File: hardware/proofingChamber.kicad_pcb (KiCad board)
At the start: 2 copper layers, 40 x 67.5 mm, 15 parts, among them J4 Conn_01x02, SW2 RotaryEncoder_Switch_MP, U1 ESP32-C3_SUPERMINI_TH, U2 DS18B20

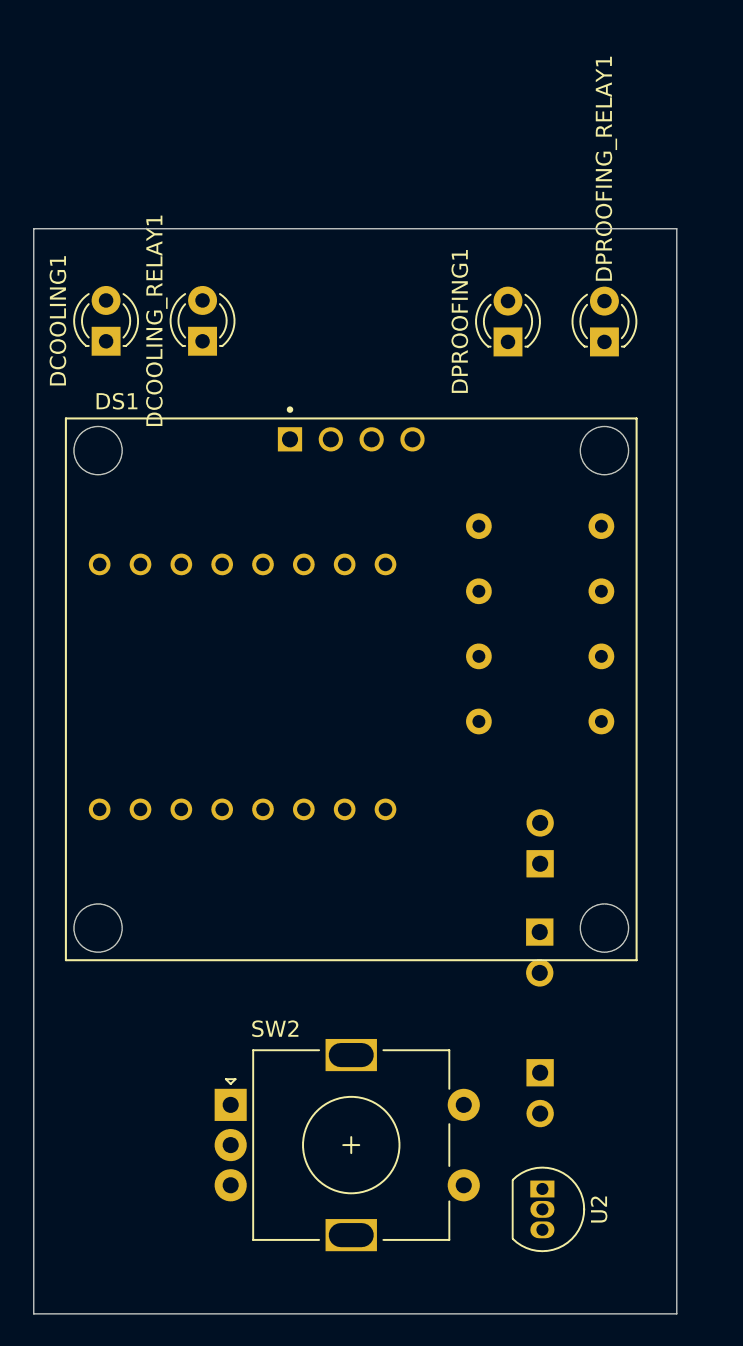
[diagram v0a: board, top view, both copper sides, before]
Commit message: Refactor hardware design files: remove obsolete proofingChamber.kicad_prl, update net classes and schematic connections
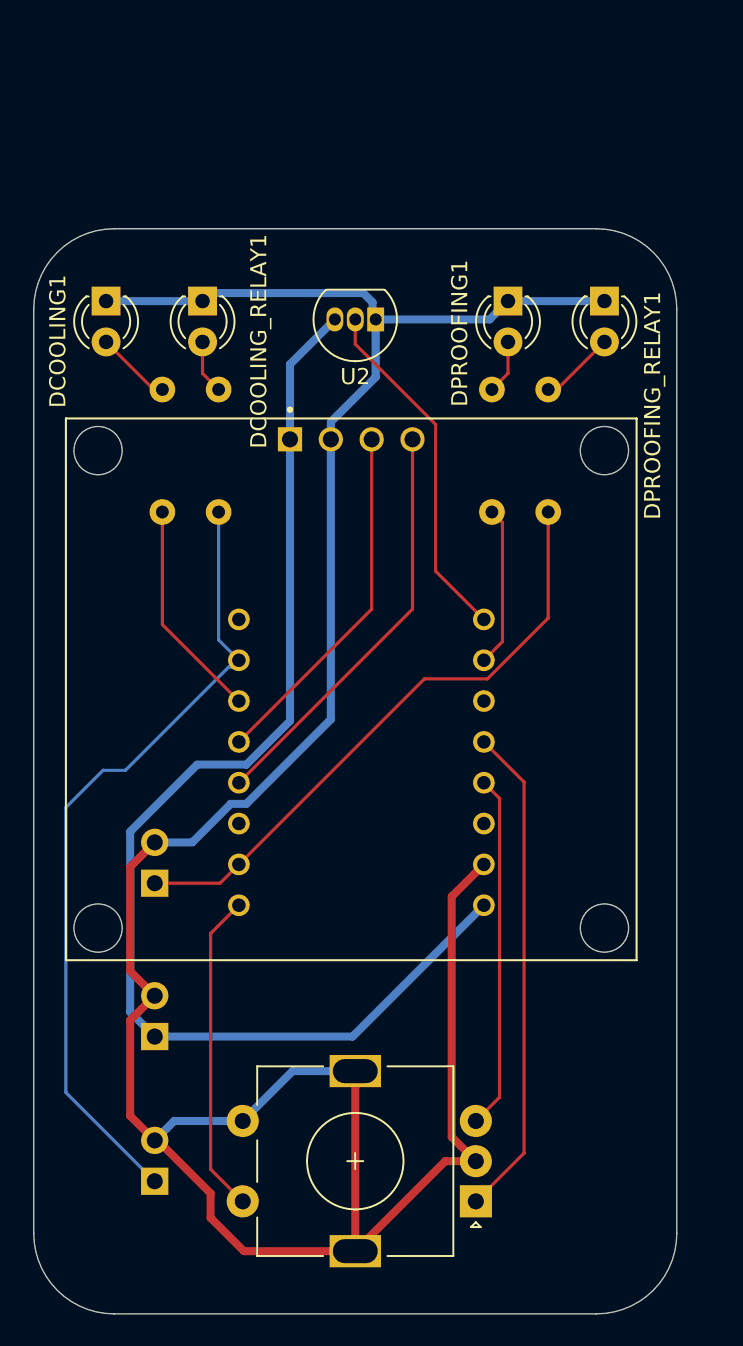
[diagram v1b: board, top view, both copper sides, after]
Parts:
- moved U2 55.1 mm to (238.8, 102.6), turned to 180 degrees
- moved RCOOLING_RELAY_LED1 31.5 mm to (229.0, 107.0), turned to -90 degrees
- moved JCOOLING1 28.5 mm to (225.0, 156.2), turned to 0 degrees
- moved JPOWER 24.1 mm to (225.0, 147.2), turned to 0 degrees
- moved JPROOFING 24.0 mm to (225.0, 137.7)
- moved RCOOLING_LED1 23.3 mm to (225.5, 107.0), turned to -90 degrees
- moved RPROOFING_RELAY_LED1 16.9 mm to (249.5, 107.0), turned to -90 degrees
- moved SW2 16.4 mm to (245.0, 157.5), turned to 180 degrees
- moved RPROOFING_LED1 10.9 mm to (246.0, 107.0), turned to -90 degrees
- moved U1 7.37 mm to (237.9, 129.2), turned to 0 degrees
- moved DPROOFING1 2.54 mm to (247.0, 101.5), turned to -90 degrees
- moved DPROOFING_RELAY1 2.54 mm to (253.0, 101.5), turned to -90 degrees
- moved DCOOLING1 2.50 mm to (222.0, 101.5), turned to -90 degrees
- moved DCOOLING_RELAY1 2.50 mm to (228.0, 101.5), turned to -90 degrees
- renumbered J4 to JPOWER, JPROOFING1 to JPROOFING
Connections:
- U1 pad 1: /COOLING_RELAY -> /PROOFING_LED
- U1 pad 2: /PROOFING_RELAY -> unconnected-(U1-GPIO2-Pad2)
- U1 pad 20: unconnected-(U1-GPIO20-Pad20) -> /COOLING_RELAY
- U1 pad 6: /PROOFING_LED -> /PROOFING_RELAY
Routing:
- net GND: track 0.00 -> 165.5 mm
- net +5V: track 0.00 -> 76.2 mm
- net /COOLING_RELAY: track 0.00 -> 49.8 mm
- net /PROOFING_RELAY: track 0.00 -> 37.5 mm
- net /ENCODER_A: track 0.00 -> 30.9 mm
- net /SDA: track 0.00 -> 25.8 mm
- net /SCK: track 0.00 -> 22.2 mm
- net /ENCODER_B: track 0.00 -> 22.1 mm
- net /DS18B22_PIN: track 0.00 -> 22.0 mm
- net /ENCODER_BTN: track 0.00 -> 20.0 mm
- net /COOLING_LED: track 0.00 -> 13.7 mm
- net /PROOFING_LED: track 0.00 -> 9.97 mm
- net Net-(DPROOFING_RELAY1-A): track 0.00 -> 4.73 mm
- net Net-(DCOOLING1-A): track 0.00 -> 4.73 mm
- net Net-(DPROOFING1-A): track 0.00 -> 3.37 mm
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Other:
- outline, holes or cut-outs redrawn

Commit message: Update PCB
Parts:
- removed DCOOLING_RELAY1, DPROOFING_RELAY1: LED, LED_THT:LED_D3.0mm
- removed JCOOLING1, JPOWER, JPROOFING: Conn_01x02, Connector_PinSocket_2.54mm:PinSocket_1x02_P2.54mm_Vertical
- removed RCOOLING_RELAY_LED1, RPROOFING_RELAY_LED1: R, Resistor_THT:R_Axial_DIN0207_L6.3mm_D2.5mm_P7.62mm_Horizontal
- removed U2: DS18B20, Package_TO_SOT_THT:TO-92_Inline
- added J1: Conn_02x06_Odd_Even, Connector_PinSocket_2.54mm:PinSocket_2x06_P2.54mm_Horizontal, B.Cu at (231.5, 131.8)
- added REF**: OSHW-Logo2_9.8x8mm_SilkScreen, Symbol:OSHW-Logo2_9.8x8mm_SilkScreen, B.Cu at (238.8, 154.0)
- moved DPROOFING1 54.1 mm to (253.0, 155.3), turned to 90 degrees
- moved DCOOLING1 53.8 mm to (224.0, 155.3), turned to 90 degrees
- moved RPROOFING_LED1 38.9 mm to (251.4, 145.5), turned to 180 degrees
- moved RCOOLING_LED1 38.5 mm to (225.5, 145.5), turned to 0 degrees
- moved SW2 15.0 mm to (231.2, 151.5), turned to 0 degrees
- moved U1 8.46 mm to (245.5, 125.5), turned to 90 degrees
- moved DS1 1.25 mm to (238.5, 125.7)
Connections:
- U1 pad 0: /DS18B22_PIN -> unconnected-(U1-GPIO0-Pad0)
- U1 pad 1: /PROOFING_LED -> /PROOFING_RELAY
- U1 pad 10: /COOLING_LED -> /PROOFING_LED
- U1 pad 2: unconnected-(U1-GPIO2-Pad2) -> /COOLING_RELAY
- U1 pad 20: /COOLING_RELAY -> /DS18B22_PIN
- U1 pad 21: unconnected-(U1-GPIO21-Pad21) -> /COOLING_LED
- U1 pad 3: /ENCODER_A -> unconnected-(U1-GPIO3-Pad3)
- U1 pad 4: /ENCODER_B -> unconnected-(U1-GPIO4-Pad4)
- U1 pad 6: /PROOFING_RELAY -> /ENCODER_B
- U1 pad 7: unconnected-(U1-GPIO7-Pad7) -> /ENCODER_A
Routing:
- net GND: track 165.5 -> 122.2 mm
- net +5V: track 76.2 -> 40.9 mm
- net /COOLING_RELAY: track 49.8 -> 16.0 mm
- net /PROOFING_RELAY: track 37.5 -> 12.5 mm
- net /DS18B22_PIN: track 22.0 -> 8.57 mm
- net /ENCODER_B: track 22.1 -> 35.4 mm
- net Net-(DPROOFING_RELAY1-A): track 4.73 -> 0.00 mm
- net Net-(DPROOFING1-A): track 3.37 -> 7.90 mm
- net Net-(DCOOLING_RELAY1-A): track 3.37 -> 0.00 mm
- net Net-(DCOOLING1-A): track 4.73 -> 7.84 mm
- net /SCK: track 22.2 -> 25.3 mm
- net /PROOFING_LED: track 9.97 -> 12.8 mm
- net /ENCODER_BTN: track 20.0 -> 22.4 mm
- net /ENCODER_A: track 30.9 -> 31.4 mm
- net /SDA: track 25.8 -> 25.3 mm
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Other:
- board size 40 x 67.5 mm -> 42 x 58.5 mm
